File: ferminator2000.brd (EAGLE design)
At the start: 111.2 x 58 mm, 120 parts, among them CN1 MINIB, IC1 FT232RL, IC2 REF01D, Q1 STP5NA50, Q2 STP5NA50, SW1 ENCODER_SW1-PEC12, U1 DSPIC33FJ256GP510A, U2 AD8495

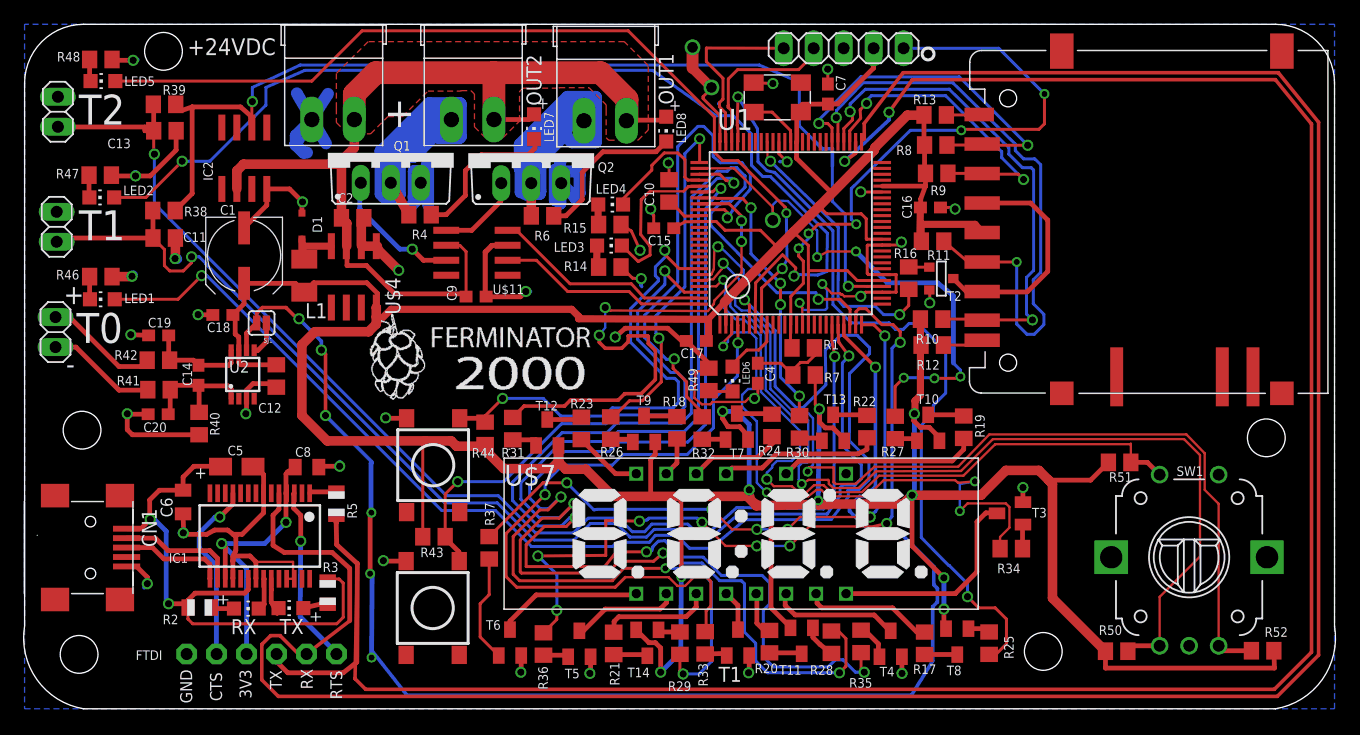
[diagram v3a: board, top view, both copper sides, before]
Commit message: Added RTC to hardware
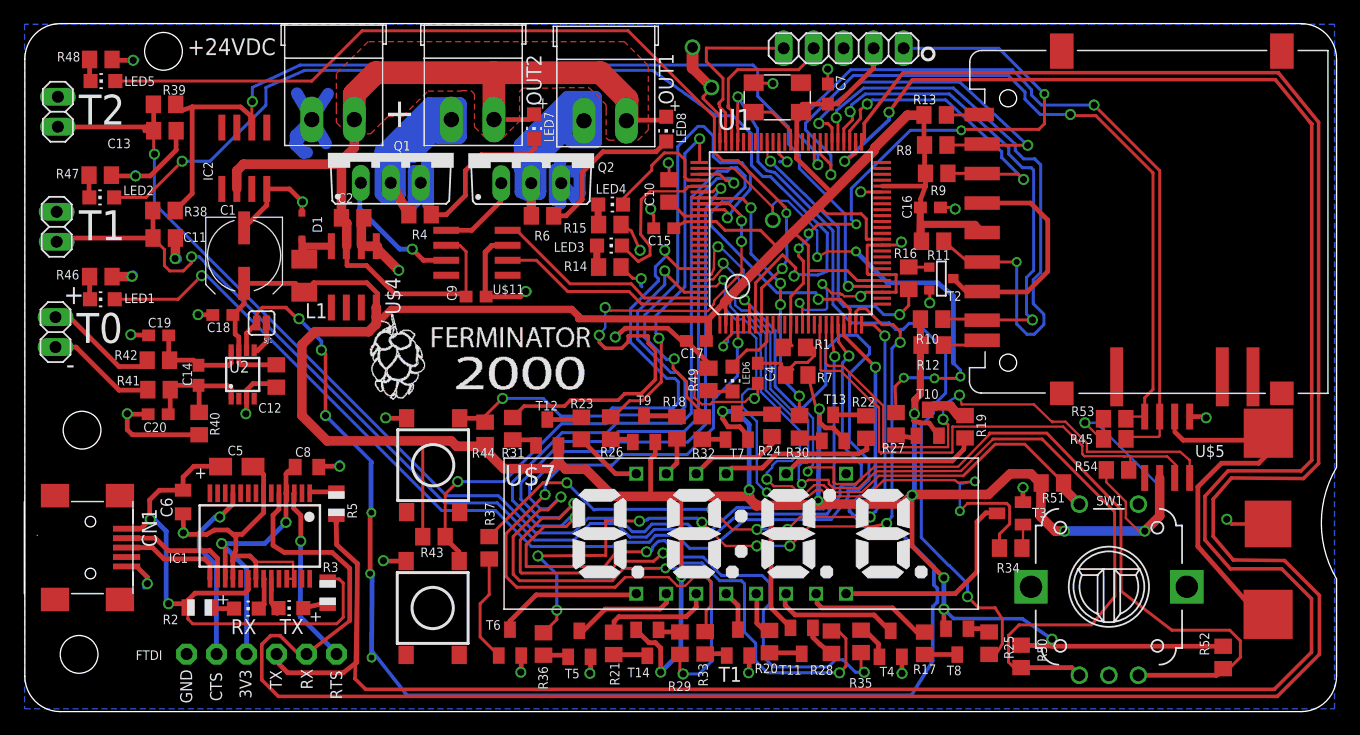
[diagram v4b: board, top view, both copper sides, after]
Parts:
- added R45, R53, R54: 10k, rcl:R0805
- added U$2: 12MM_BATTER_HOLDER, eric_sorensen:12.5MMCOILCELLHOLDER
- added U$5: DS3231, eric_sorensen:SOIC8
- moved R50 8.11 mm to (86.1, 4.98), turned to 270 degrees
- moved SW1 7.24 mm to (93.6, 10.9)
- moved R51 5.96 mm to (88.8, 19.7)
- moved R52 3.40 mm to (103.2, 4.89), turned to 270 degrees
- moved R1 0.75 mm to (66.9, 31.2)
- moved R7 0.62 mm to (67.1, 28.8)
- moved T10 0.43 mm to (78.2, 24.8)
- moved R27 0.32 mm to (75.5, 24.7)
- moved R19 0.12 mm to (81.4, 24.4)
- moved R22 0.10 mm to (73.0, 24.4)
- moved R34 0.07 mm to (85.2, 14.2)
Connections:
- new net N$22: U$2.P$2, U$2.P$3, U$5.6
- new net N$23: R45.1, U$5.7, U1.59
- new net N$60: R53.1, U$5.8, U1.58
- new net RST_INT: U$5.4, U1.19
- new net RTC_INT: R54.1, U$5.3, U1.18
- net GND: now also U$2.P$1, U$5.5
- net VDD: now also R45.2, R53.2, R54.2, U$5.2
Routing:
- net N$23: track 0.00 -> 68.2 mm, vias 0 -> 2
- net N$60: track 0.00 -> 65.9 mm, vias 0 -> 2
- net RST_INT: track 0.00 -> 48.0 mm, vias 0 -> 2
- net RTC_INT: track 0.00 -> 45.4 mm
- net N$22: track 0.00 -> 32.9 mm
- net VDD: track 393.6 -> 424.2 mm, vias 10 -> 14
- net TX: track 210.4 -> 224.2 mm
- net RX: track 209.6 -> 223.1 mm
- net N$57: track 85.6 -> 97.2 mm
- net N$59: track 62.1 -> 55.6 mm
- net GND: track 225.6 -> 231.2 mm, vias 39 -> 41
- net +2.5VREF: track 90.1 -> 88.5 mm
- net N$6: track 6.84 -> 8.27 mm
- net N$58: track 84.1 -> 84.8 mm
- net 3: track 3.11 -> 3.80 mm
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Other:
- board size 111.2 x 58 mm -> 111.1 x 58.3 mm
